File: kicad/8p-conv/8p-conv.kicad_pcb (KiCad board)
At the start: 2 copper layers, 20.3 x 12.7 mm, 2 parts, among them J1 Conn_01x08, J2 Conn_01x08

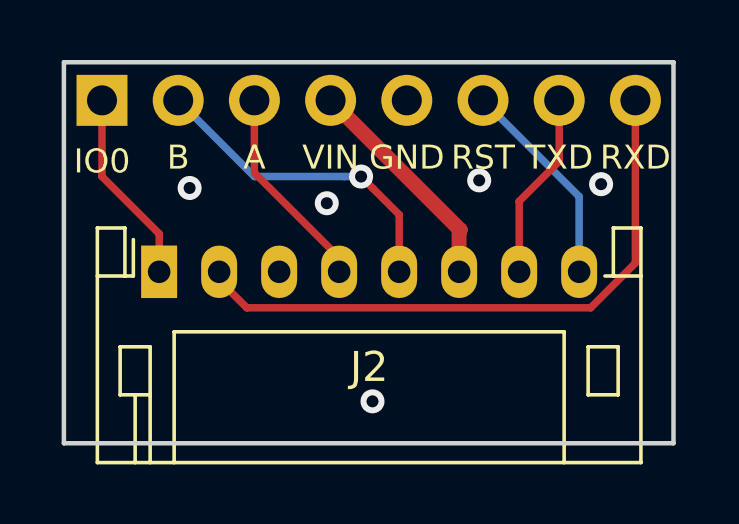
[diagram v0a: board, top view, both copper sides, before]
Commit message: 8p-PH conversion board for esp32-devboard
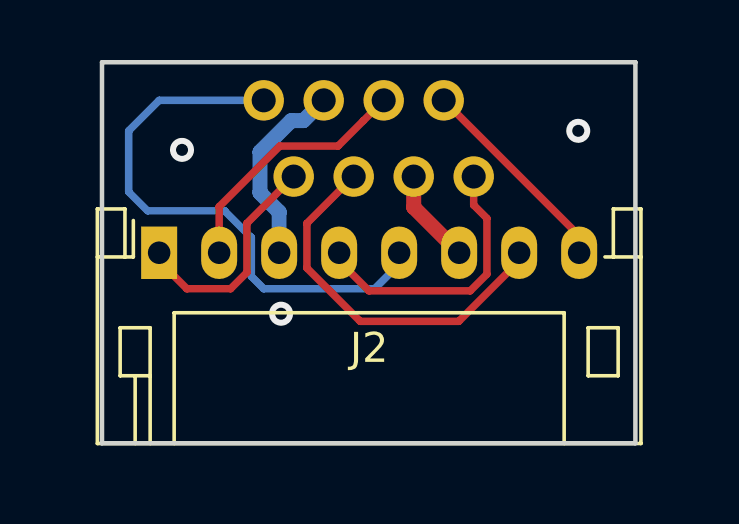
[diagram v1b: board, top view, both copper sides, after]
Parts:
- added J3: Conn_01x04, Connector_PinHeader_2.00mm:PinHeader_1x04_P2.00mm_Vertical, B.Cu at (149.9, 54.6)
- J1: value Conn_01x08 -> Conn_01x04; footprint Connector_PinHeader_2.54mm:PinHeader_1x08_P2.54mm_Vertical -> Connector_PinHeader_2.00mm:PinHeader_1x04_P2.00mm_Vertical
- moved J1 5.39 mm to (148.9, 52.1)
- moved J2 0.63 mm to (145.4, 57.1)
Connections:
- J1 pad 1: /IO0 -> /B
- J1 pad 2: /B -> /GND
- J1 pad 3: /A -> /RXD
- J1 pad 4: /VIN -> /RST
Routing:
- net /RXD: track 20.6 -> 8.49 mm
- net /B: track 10.8 -> 18.8 mm, vias 1 -> 0
- net /GND: track 0.00 -> 6.46 mm, vias 5 -> 3
- net /TXD: track 6.27 -> 12.6 mm
- net /VIN: track 7.52 -> 3.17 mm
- net /A: track 6.89 -> 9.28 mm
- net /IO0: track 6.50 -> 7.65 mm
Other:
- board size 20.3 x 12.7 mm -> 17.8 x 12.7 mm
